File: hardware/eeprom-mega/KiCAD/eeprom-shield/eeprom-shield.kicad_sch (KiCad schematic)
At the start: 15 parts, among them J1 Power, J2 PWM, J3 Analog, J4 PWM, J5 Analog, J6 Communication, J7 Digital, SW1 SW_SPST, U1 28C256

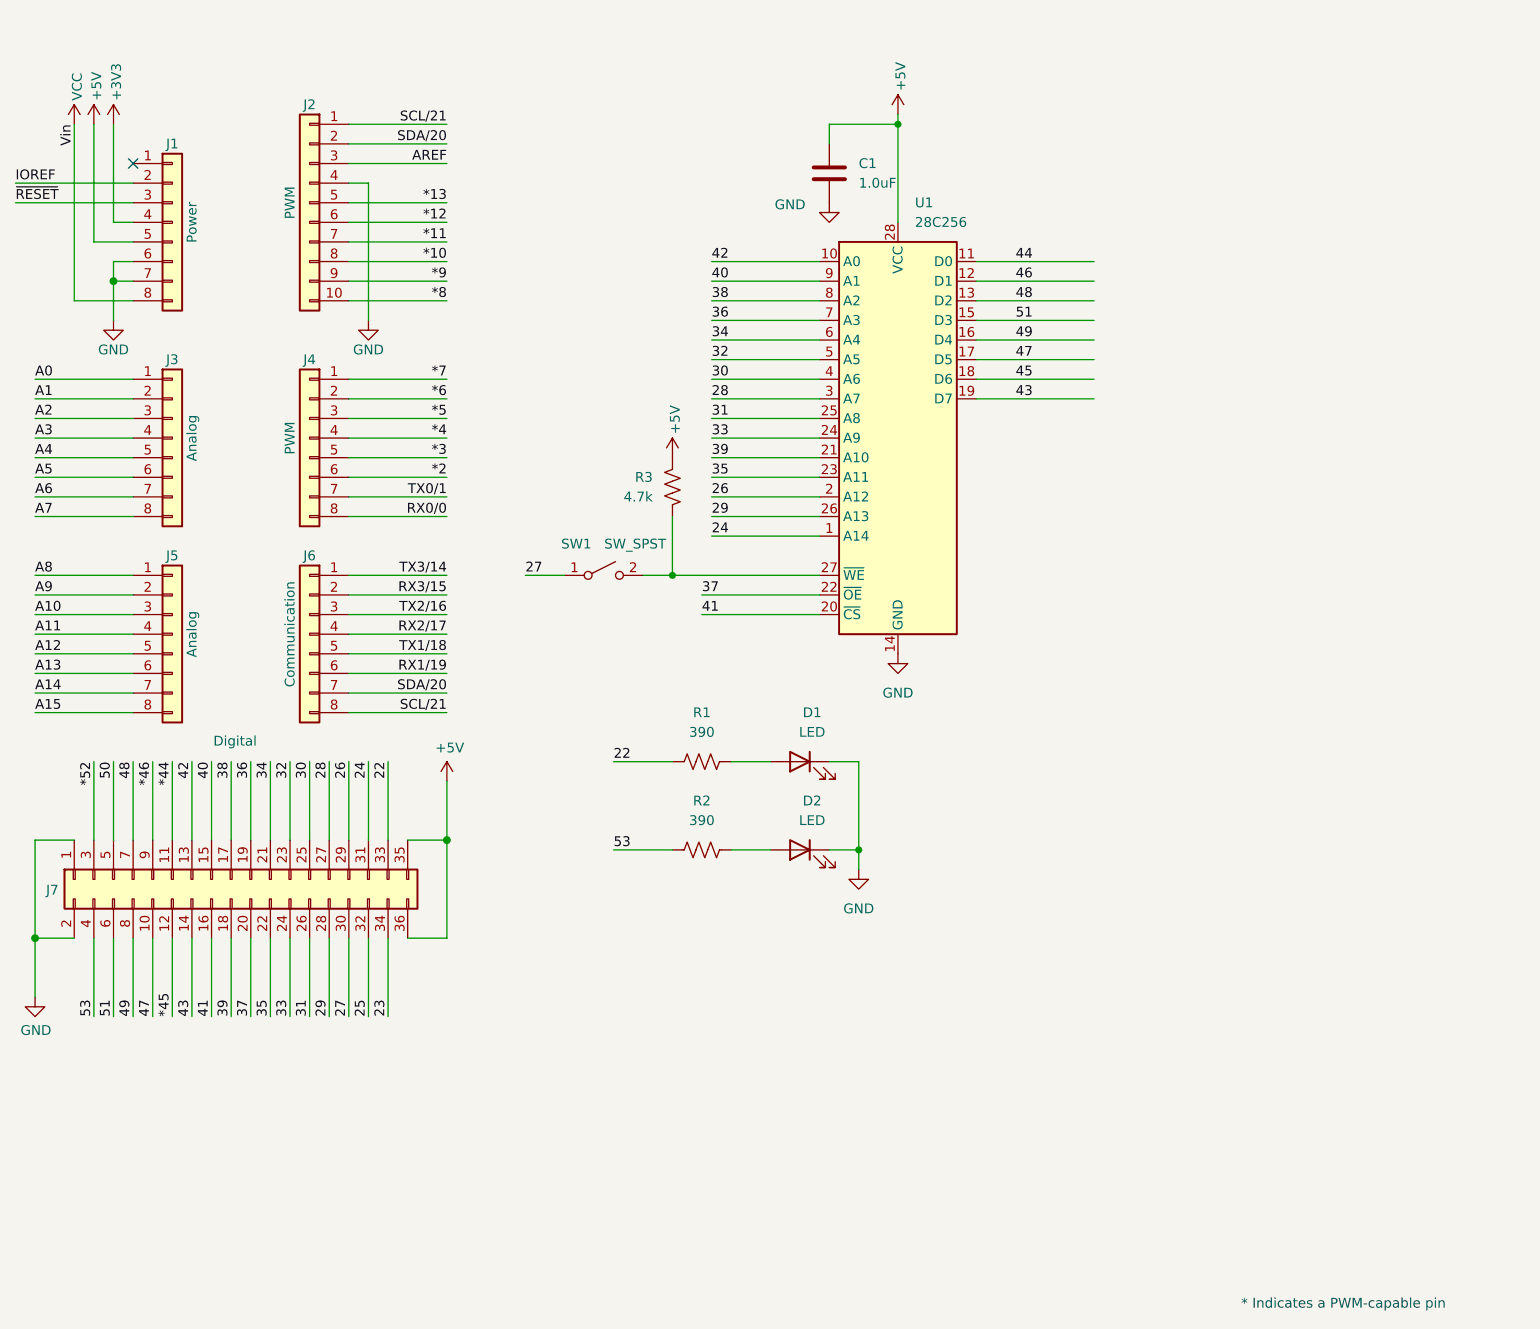
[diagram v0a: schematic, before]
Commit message: EEPROM shield as built, arduino code to drive
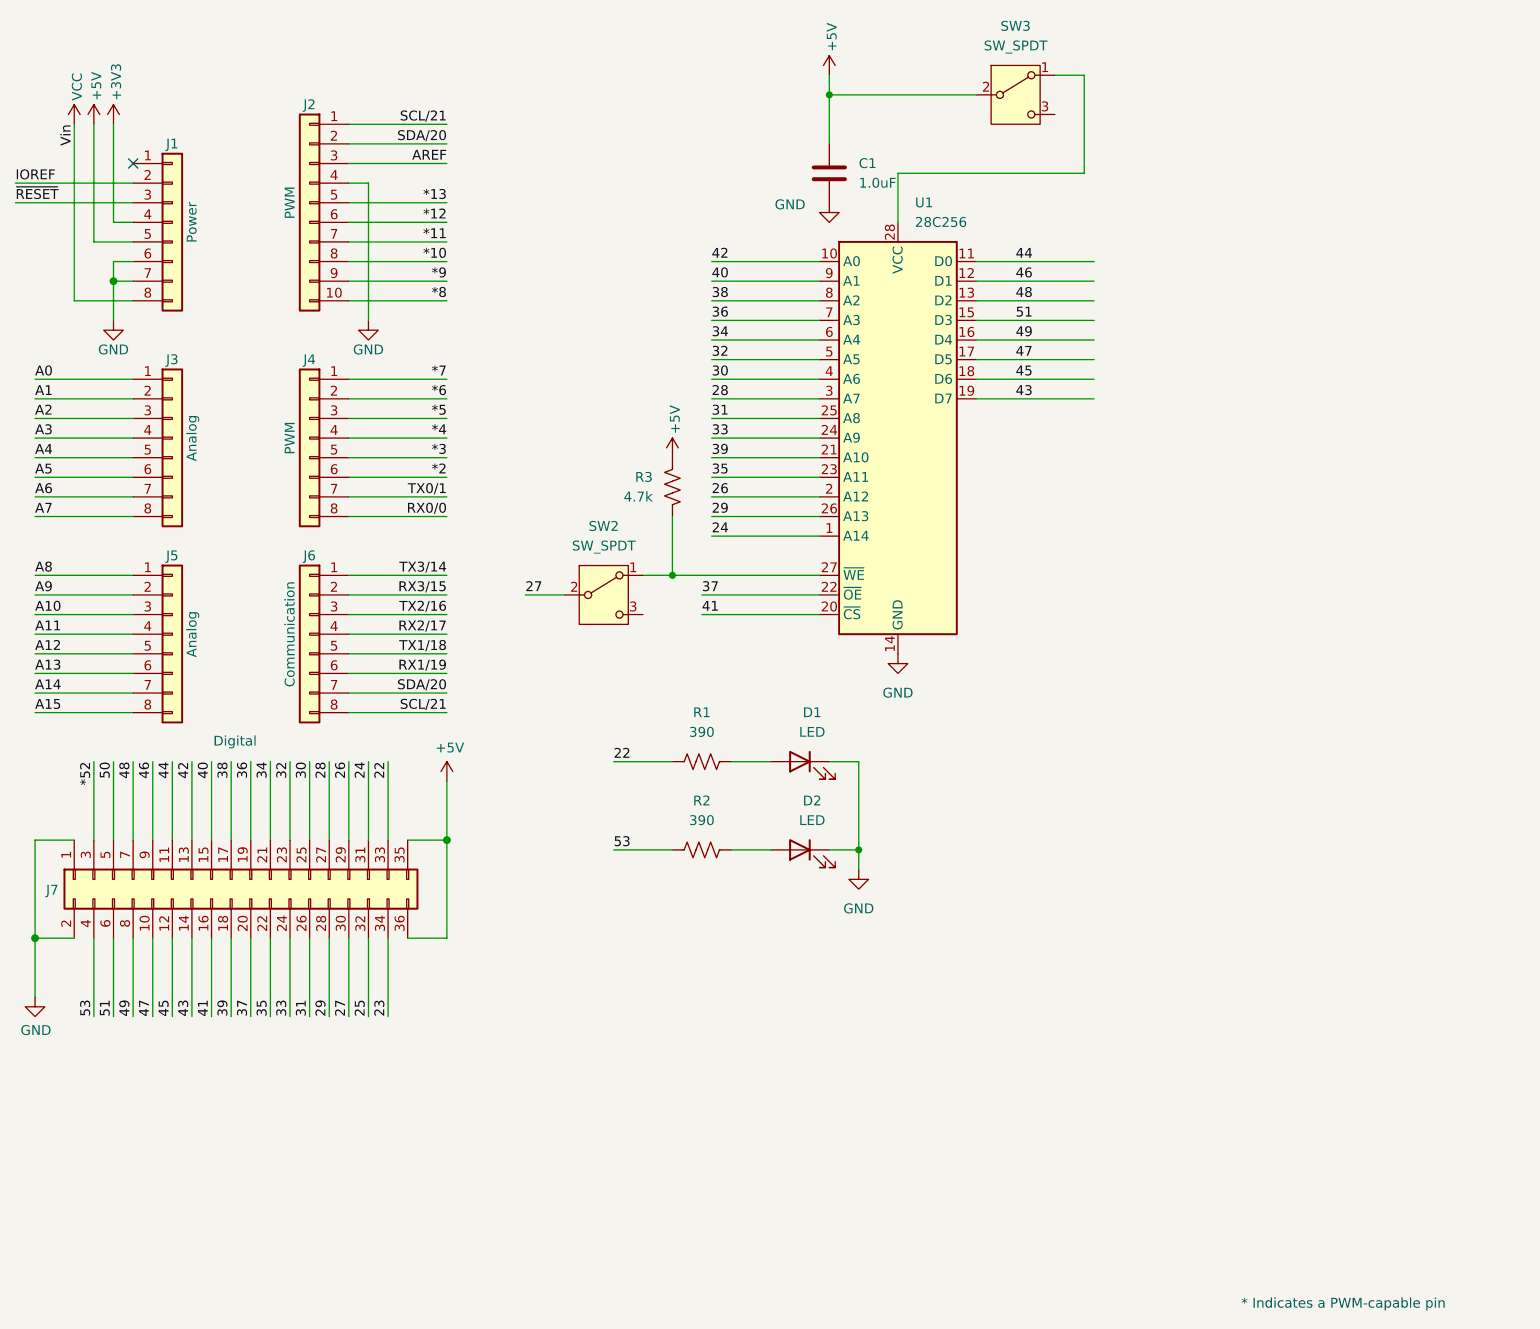
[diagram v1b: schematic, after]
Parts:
- removed SW1: SW_SPST, Connector_PinHeader_2.54mm:PinHeader_1x02_P2.54mm_Vertical, symbol Switch:SW_SPST
- added SW2, SW3: SW_SPDT, my_slide_sw:sw_spdt_2.54mm, symbol Switch:SW_SPDT
- U1: footprint Package_DIP:DIP-28_W15.24mm_Socket_LongPads -> my_zif_28:DIP_Socket-28_W11.9_W12.7_W15.24_W17.78_W18.5_3M_228-1277-00-0602J
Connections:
- net *44 is gone; now on net 44: J7.11 (Pin_11)
- net *45 is gone; now on net 45: J7.12 (Pin_12)
- net *46 is gone; now on net 46: J7.9 (Pin_9)
- net +5V: now also SW3.2 (B); no longer U1.28 (VCC)
- net 27: now also SW2.2 (B)
- net at R3.1, U1.27 (~{WE}): now also SW2.1 (A)
- new net: SW3.1 (A), U1.28 (VCC)
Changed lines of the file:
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@@
 	)
 	(junction
-		(at 31.75 46.99)
-		(diameter 1.016)
+		(at 124.46 22.86)
+		(diameter 0)
 		(color 0 0 0 0)
 	)
 	(junction
-		(at 133.35 26.67)
-		(diameter 0)
+		(at 31.75 46.99)
+		(diameter 1.016)
 		(color 0 0 0 0)
 	)
@@
 	(wire
 		(pts
+			(xy 133.35 33.02) (xy 157.48 33.02)
+		)
+		(stroke
+			(width 0)
+			(type default)
+		)
+	)
+	(wire
+		(pts
 			(xy 96.52 109.22) (xy 104.14 109.22)
 		)
@@
 	(wire
 		(pts
-			(xy 133.35 26.67) (xy 133.35 39.37)
+			(xy 54.61 109.22) (xy 54.61 119.38)
 		)
 		(stroke
 			(width 0)
-			(type default)
+			(type solid)
 		)
 	)
 	(wire
 		(pts
-			(xy 54.61 109.22) (xy 54.61 119.38)
+			(xy 31.75 109.22) (xy 31.75 119.38)
 		)
 		(stroke
@@
 	(wire
 		(pts
-			(xy 31.75 109.22) (xy 31.75 119.38)
+			(xy 67.31 109.22) (xy 67.31 119.38)
 		)
 		(stroke
@@
 	(wire
 		(pts
-			(xy 67.31 109.22) (xy 67.31 119.38)
+			(xy 124.46 22.86) (xy 143.51 22.86)
 		)
 		(stroke
 			(width 0)
-			(type solid)
+			(type default)
 		)
 	)
@@
 	(wire
 		(pts
-			(xy 133.35 25.4) (xy 133.35 26.67)
+			(xy 124.46 20.32) (xy 124.46 22.86)
 		)
 		(stroke
@@
 	(wire
 		(pts
-			(xy 124.46 29.21) (xy 124.46 26.67)
-		)
-		(stroke
-			(width 0)
-			(type default)
-		)
-	)
-	(wire
-		(pts
 			(xy 124.46 120.65) (xy 128.27 120.65)
 		)
@@
 	(wire
 		(pts
-			(xy 85.09 85.09) (xy 90.17 85.09)
+			(xy 85.09 87.63) (xy 90.17 87.63)
 		)
 		(stroke
@@
 	(wire
 		(pts
+			(xy 124.46 22.86) (xy 124.46 29.21)
+		)
+		(stroke
+			(width 0)
+			(type default)
+		)
+	)
+	(wire
+		(pts
 			(xy 64.77 34.29) (xy 64.77 52.07)
 		)
@@
 	(wire
 		(pts
+			(xy 157.48 20.32) (xy 157.48 33.02)
+		)
+		(stroke
+			(width 0)
+			(type default)
+		)
+	)
+	(wire
+		(pts
 			(xy 143.51 57.15) (xy 158.75 57.15)
 		)
@@
 	(wire
 		(pts
+			(xy 153.67 20.32) (xy 157.48 20.32)
+		)
+		(stroke
+			(width 0)
+			(type default)
+		)
+	)
+	(wire
+		(pts
 			(xy 34.29 49.53) (xy 26.67 49.53)
 		)
@@
 	(wire
 		(pts
-			(xy 34.29 85.09) (xy 21.59 85.09)
+			(xy 133.35 39.37) (xy 133.35 33.02)
 		)
 		(stroke
 			(width 0)
-			(type solid)
+			(type default)
 		)
 	)
 	(wire
 		(pts
-			(xy 143.51 49.53) (xy 158.75 49.53)
+			(xy 34.29 85.09) (xy 21.59 85.09)
 		)
 		(stroke
 			(width 0)
-			(type default)
+			(type solid)
 		)
 	)
 	(wire
 		(pts
-			(xy 67.31 132.08) (xy 67.31 142.24)
+			(xy 143.51 49.53) (xy 158.75 49.53)
 		)
 		(stroke
 			(width 0)
-			(type solid)
+			(type default)
 		)
 	)
 	(wire
 		(pts
-			(xy 124.46 26.67) (xy 133.35 26.67)
+			(xy 67.31 132.08) (xy 67.31 142.24)
 		)
 		(stroke
 			(width 0)
-			(type default)
+			(type solid)
 		)
 	)
@@
 		)
 	)
-	(label "*44"
+	(label "44"
 		(at 39.37 109.22 270)
 		(fields_autoplaced yes)
@@
 		)
 	)
-	(label "*45"
+	(label "45"
 		(at 39.37 142.24 90)
 		(fields_autoplaced yes)
@@
 		)
 	)
-	(label "*46"
+	(label "46"
 		(at 36.83 109.22 270)
 		(fields_autoplaced yes)
@@
 	)
 	(label "27"
-		(at 85.09 85.09 0)
+		(at 85.09 87.63 0)
 		(fields_autoplaced yes)
 		(effects
@@
 	)
 	(symbol
+		(lib_id "Switch:SW_SPDT")
+		(at 95.25 87.63 0)
+		(unit 1)
+		(exclude_from_sim no)
+		(in_bom yes)
+		(on_board yes)
+		(dnp no)
+		(fields_autoplaced yes)
+		(property "Reference" "SW2"
+			(at 95.25 78.74 0)
+			(effects
+				(font
+					(size 1.27 1.27)
+				)
+			)
+		)
+		(property "Value" "SW_SPDT"
+			(at 95.25 81.28 0)
+			(effects
+				(font
+					(size 1.27 1.27)
+				)
+			)
+		)
+		(property "Footprint" "my_slide_sw:sw_spdt_2.54mm"
+			(at 95.25 87.63 0)
+			(effects
+				(font
+					(size 1.27 1.27)
+				)
+				(hide yes)
+			)
+		)
+		(property "Datasheet" "~"
+			(at 95.25 95.25 0)
+			(effects
+				(font
+					(size 1.27 1.27)
+				)
+				(hide yes)
+			)
+		)
+		(property "Description" "Switch, single pole double throw"
+			(at 95.25 87.63 0)
+			(effects
+				(font
+					(size 1.27 1.27)
+				)
+				(hide yes)
+			)
+		)
+		(pin "2"
+		)
+		(pin "1"
+		)
+		(pin "3"
+		)
+		(instances
+			(project "eeprom-shield"
+				(path "/e63e39d7-6ac0-4ffd-8aa3-1841a4541b55"
+					(reference "SW2")
+					(unit 1)
+				)
+			)
+		)
+	)
+	(symbol
 		(lib_id "Device:R_US")
 		(at 107.95 120.65 90)
@@
 			)
 		)
-		(property "Footprint" "Package_DIP:DIP-28_W15.24mm_Socket_LongPads"
+		(property "Footprint" "my_zif_28:DIP_Socket-28_W11.9_W12.7_W15.24_W17.78_W18.5_3M_228-1277-00-0602J"
 			(at 133.35 67.31 0)
 			(effects
@@
 	(symbol
 		(lib_id "power:+5V")
-		(at 133.35 25.4 0)
+		(at 124.46 20.32 0)
 		(unit 1)
 		(exclude_from_sim no)
@@
 		(dnp no)
 		(property "Reference" "#PWR010"
-			(at 133.35 29.21 0)
+			(at 124.46 24.13 0)
 			(effects
 				(font
@@
 		)
 		(property "Value" "+5V"
-			(at 133.7056 22.352 90)
+			(at 124.8156 17.272 90)
 			(effects
 				(font
@@
 		)
 		(property "Footprint" ""
-			(at 133.35 25.4 0)
+			(at 124.46 20.32 0)
 			(effects
 				(font
@@
 		)
 		(property "Datasheet" ""
-			(at 133.35 25.4 0)
+			(at 124.46 20.32 0)
 			(effects
 				(font
@@
 		)
 		(property "Description" ""
-			(at 133.35 25.4 0)
+			(at 124.46 20.32 0)
 			(effects
 				(font
@@
 	)
 	(symbol
-		(lib_id "Switch:SW_SPST")
-		(at 95.25 85.09 0)
+		(lib_id "Switch:SW_SPDT")
+		(at 148.59 22.86 0)
 		(unit 1)
 		(exclude_from_sim no)
@@
 		(on_board yes)
 		(dnp no)
-		(property "Reference" "SW1"
-			(at 91.694 81.026 0)
+		(fields_autoplaced yes)
+		(property "Reference" "SW3"
+			(at 148.59 13.97 0)
 			(effects
 				(font
@@
 			)
 		)
-		(property "Value" "SW_SPST"
-			(at 99.314 81.026 0)
+		(property "Value" "SW_SPDT"
+			(at 148.59 16.51 0)
 			(effects
 				(font
@@
 			)
 		)
-		(property "Footprint" "Connector_PinHeader_2.54mm:PinHeader_1x02_P2.54mm_Vertical"
-			(at 95.25 85.09 0)
+		(property "Footprint" "my_slide_sw:sw_spdt_2.54mm"
+			(at 148.59 22.86 0)
 			(effects
 				(font
@@
 		)
 		(property "Datasheet" "~"
-			(at 95.25 85.09 0)
+			(at 148.59 30.48 0)
 			(effects
 				(font
@@
 			)
 		)
-		(property "Description" "Single Pole Single Throw (SPST) switch"
-			(at 95.25 85.09 0)
+		(property "Description" "Switch, single pole double throw"
+			(at 148.59 22.86 0)
 			(effects
 				(font
@@
 			)
 		)
+		(pin "2"
+		)
 		(pin "1"
 		)
-		(pin "2"
+		(pin "3"
 		)
 		(instances
 			(project ""
 				(path "/e63e39d7-6ac0-4ffd-8aa3-1841a4541b55"
-					(reference "SW1")
+					(reference "SW3")
 					(unit 1)
 				)
